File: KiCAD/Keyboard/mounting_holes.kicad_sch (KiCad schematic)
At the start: 10 parts

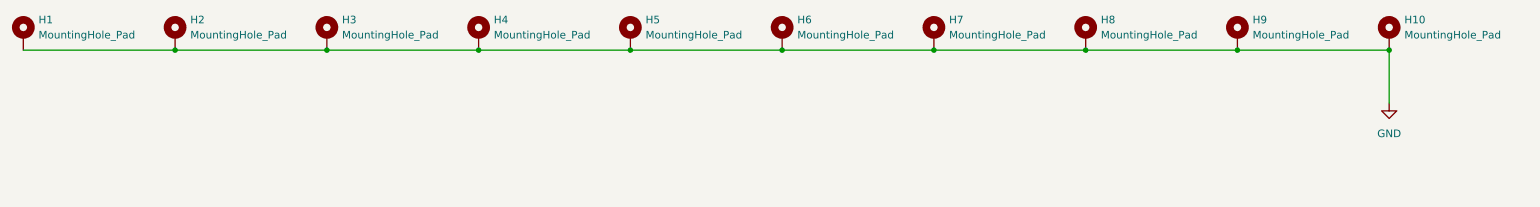
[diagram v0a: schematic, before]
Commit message: make board smaller
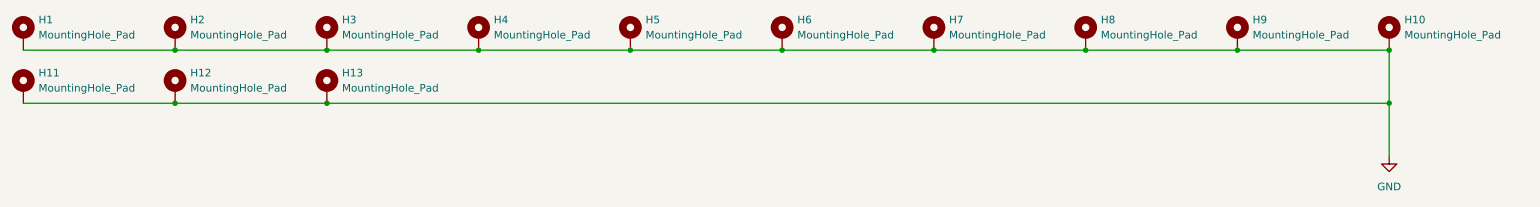
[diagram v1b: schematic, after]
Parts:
- removed H5, H6: MountingHole_Pad, MountingHole:MountingHole_2.2mm_M2_DIN965_Pad_TopBottom, symbol Mechanical:MountingHole_Pad
- added H10, H11, H12, H13, H9: MountingHole_Pad, MountingHole:MountingHole_2.2mm_M2_DIN965_Pad_TopBottom, symbol Mechanical:MountingHole_Pad
- renumbered H7 to H5, H8 to H6, H9 to H7, H10 to H8
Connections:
- net GND: now also H10.1, H11.1, H12.1, H13.1, H9.1
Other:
- moved on the sheet: H5, H6, H7, H8
